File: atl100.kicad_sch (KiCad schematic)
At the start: 0 parts

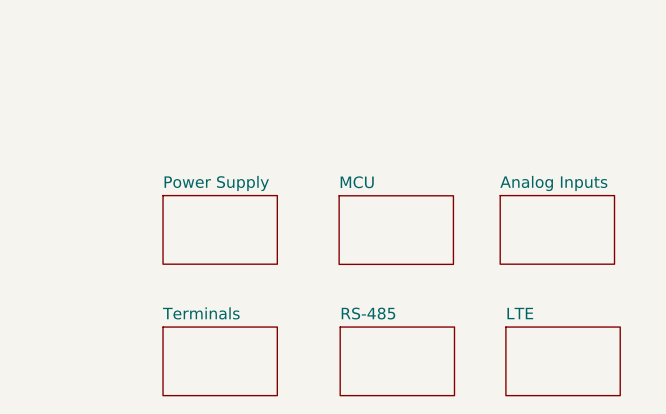
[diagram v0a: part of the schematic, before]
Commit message: feat: Main board schematic updated
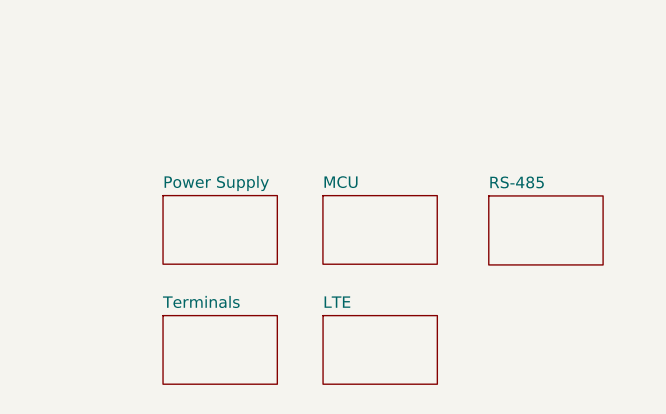
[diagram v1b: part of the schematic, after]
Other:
- removed sheet Analog Inputs
- title: ATL-100 (Multiparametric Station) -> ATL-100 (Multiparametric Station) - Main Board
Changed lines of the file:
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@@
 	(paper "A4")
 	(title_block
-		(title "ATL-100 (Multiparametric Station)")
-		(date "2025-06-01")
+		(title "ATL-100 (Multiparametric Station) - Main Board")
+		(date "2025-06-02")
 		(rev "v0.2.0")
 		(company "AgroTechLab (Agribusiness Technology Development Laboratory)")
@@
 		(comment 2 "Author: Robson Costa (robson.costa@ifsc.edu.br)")
 		(comment 3 "Licensed under CC-BY-SA 4.0")
-		(comment 4 "Total Supply Current: ??mA (??mA)")
+		(comment 4 "Max. peak supply current: 906,6mA")
 	)
 	(rectangle
@@
 	)
 	(sheet
-		(at 215.9 153.67)
+		(at 195.58 152.4)
 		(size 12.7 7.62)
 		(exclude_from_sim no)
@@
 		)
 		(property "Sheetname" "LTE"
-			(at 215.9 152.9584 0)
+			(at 195.58 151.6884 0)
 			(effects
 				(font
@@
 		)
 		(property "Sheetfile" "atl100_lte.kicad_sch"
-			(at 215.9 161.8746 0)
+			(at 195.58 160.6046 0)
 			(effects
 				(font
@@
 	)
 	(sheet
-		(at 215.265 139.065)
-		(size 12.7 7.62)
-		(exclude_from_sim no)
-		(in_bom yes)
-		(on_board yes)
-		(dnp no)
-		(fields_autoplaced yes)
-		(stroke
-			(width 0.1524)
-			(type solid)
-		)
-		(fill
-			(color 0 0 0 0.0000)
-		)
-		(property "Sheetname" "Analog Inputs"
-			(at 215.265 138.3534 0)
-			(effects
-				(font
-					(size 1.27 1.27)
-				)
-				(justify left bottom)
-			)
-		)
-		(property "Sheetfile" "atl100_ai.kicad_sch"
-			(at 215.265 147.2696 0)
-			(effects
-				(font
-					(size 1.27 1.27)
-				)
-				(justify left top)
-				(hide yes)
-			)
-		)
-		(instances
-			(project "atl100"
-				(path "/9f25808e-b525-4dd9-b9a0-a085d29b6aa9"
-					(page "6")
-				)
-			)
-		)
-	)
-	(sheet
-		(at 197.485 153.67)
-		(size 12.7 7.62)
+		(at 213.995 139.1045)
+		(size 12.7 7.6651)
 		(exclude_from_sim no)
 		(in_bom yes)
@@
 		)
 		(property "Sheetname" "RS-485"
-			(at 197.485 152.9584 0)
+			(at 213.995 138.3929 0)
 			(effects
 				(font
@@
 		)
 		(property "Sheetfile" "atl100_rs485.kicad_sch"
-			(at 197.485 161.8746 0)
+			(at 213.995 147.3542 0)
 			(effects
 				(font
@@
 	)
 	(sheet
-		(at 197.3673 139.0856)
+		(at 195.5694 139.069)
 		(size 12.7 7.62)
 		(exclude_from_sim no)
@@
 		)
 		(property "Sheetname" "MCU"
-			(at 197.3673 138.374 0)
+			(at 195.5694 138.3574 0)
 			(effects
 				(font
@@
 		)
 		(property "Sheetfile" "atl100_mcu.kicad_sch"
-			(at 197.3673 147.2902 0)
+			(at 195.5694 147.2736 0)
 			(effects
 				(font
@@
 	)
 	(sheet
-		(at 177.8 153.67)
+		(at 177.8 152.4)
 		(size 12.7 7.62)
 		(exclude_from_sim no)
@@
 		)
 		(property "Sheetname" "Terminals"
-			(at 177.8 152.9584 0)
+			(at 177.8 151.6884 0)
 			(effects
 				(font
@@
 		)
 		(property "Sheetfile" "atl100_terminals.kicad_sch"
-			(at 177.8 161.8746 0)
-			(effects
-				(font
+			(at 177.8 160.6046 0)
+			(effects
+				(font

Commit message: feat: Updated to v0.2.0
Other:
- added sheet LoRa (atl100_lora.kicad_sch)
- note added: "Internal Modules: - MCU (ESP32-S3) - XL4005 (Voltage Regulator - Step Down) - Voltage Sensor (power supply voltage) - HW-519 (RS-485) - RGB LED - RAK3272S (LoRaWAN module) - SIM7070G (LTE module) External Modules: - BME-280 (I2C port) - Air Temperature (ºC) - Air Humidity (%) - Atmospherical Pressure (mmHg) - Pluviometer (pulse port) - Rain Amount (mm) - Anemometer (pulse port) - Wind Speed (m/se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"
- note removed: "Internal Modules: - MCU (ESP32-S3) - XL4005 (Voltage Regulator - Step Down) - Voltage Sensor (power supply voltage) - HW-519 (RS-485) - RGB LED External Modules: - BME-280 (I2C port) - Air Temperature (ºC) - Air Humidity (%) - Atmospherical Pressure (mmHg) - Pluviometer (pulse port) - Rain Amount (mm) - Anemometer (pulse port) - Wind Speed (m/sec. or Km/h) - Windsock (ADC port) - Wind Direction (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"
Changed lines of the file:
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@@
 	(title_block
 		(title "ATL-100 (Multiparametric Station) - Main Board")
-		(date "2025-06-02")
+		(date "2025-06-05")
 		(rev "v0.2.0")
 		(company "AgroTechLab (Agribusiness Technology Development Laboratory)")
@@
 	(rectangle
 		(start 31.115 34.29)
-		(end 106.68 95.25)
+		(end 106.68 99.06)
 		(stroke
 			(width 0)
@@
 		)
 	)
-	(text "Internal Modules:\n   - MCU (ESP32-S3)\n   - XL4005 (Voltage Regulator - Step Down)\n   - Voltage Sensor (power supply voltage)\n   - HW-519 (RS-485)\n   - RGB LED\n\nExternal Modules:\n   - BME-280 (I2C port)\n      - Air Temperature (ºC)\n      - Air Humidity (%)\n      - Atmospherical Pressure (mmHg)\n   - Pluviometer (pulse port)\n      - Rain Amount (mm)\n   - Anemometer (pulse port)\n      - Wind Speed (m/sec. or Km/h)\n   - Windsock (ADC port)\n      - Wind Direction (N, NE, E, SE, S, SW, W, NW)\n   - ADC 4mA - 20mA (4x ports)\n   - Soil Sensor (RS-485 port)\n      - Temperature (%)\n      - Moisture (ºC)\n      - PH (index)\n      - Conductivity (µs/cm)\n      - Nitrogen (mg/Kg)\n      - Phosphorus (mg/Kg)\n      - Potassium (mg/Kg)"
+	(text "Internal Modules:\n   - MCU (ESP32-S3)\n   - XL4005 (Voltage Regulator - Step Down)\n   - Voltage Sensor (power supply voltage)\n   - HW-519 (RS-485)\n   - RGB LED\n   - RAK3272S (LoRaWAN module)\n   - SIM7070G (LTE module)\n\nExternal Modules:\n   - BME-280 (I2C port)\n      - Air Temperature (ºC)\n      - Air Humidity (%)\n      - Atmospherical Pressure (mmHg)\n   - Pluviometer (pulse port)\n      - Rain Amount (mm)\n   - Anemometer (pulse port)\n      - Wind Speed (m/sec. or Km/h)\n   - Windsock (ADC port)\n      - Wind Direction (N, NE, E, SE, S, SW, W, NW)\n   - ADC 4mA - 20mA (4x ports)\n   - Soil Sensor (RS-485 port)\n      - Temperature (%)\n      - Moisture (ºC)\n      - PH (index)\n      - Conductivity (µs/cm)\n      - Nitrogen (mg/Kg)\n      - Phosphorus (mg/Kg)\n      - Potassium (mg/Kg)"
 		(exclude_from_sim no)
-		(at 33.528 93.726 0)
+		(at 33.528 97.282 0)
 		(effects
 			(font
@@
 			(effects
 				(font
+					(size 1.27 1.27)
+				)
+				(justify left top)
+				(hide yes)
+			)
+		)
+		(instances
+			(project "atl100"
+				(path "/9f25808e-b525-4dd9-b9a0-a085d29b6aa9"
+					(page "6")
+				)
+			)
+		)
+	)
+	(sheet
+		(at 213.7902 152.4479)
+		(size 12.7 7.62)
+		(exclude_from_sim no)
+		(in_bom yes)
+		(on_board yes)
+		(dnp no)
+		(fields_autoplaced yes)
+		(stroke
+			(width 0.1524)
+			(type solid)
+		)
+		(fill
+			(color 0 0 0 0.0000)
+		)
+		(property "Sheetname" "LoRa"
+			(at 213.7902 151.7363 0)
+			(effects
+				(font
+					(size 1.27 1.27)
+				)
+				(justify left bottom)
+			)
+		)
+		(property "Sheetfile" "atl100_lora.kicad_sch"
+			(at 213.7902 160.6525 0)
+			(effects
+				(font
